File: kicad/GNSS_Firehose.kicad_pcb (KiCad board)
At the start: 4 copper layers, 117.9 x 99.1 mm, 474 parts, among them J1 SMA, J10 HEADER_16, J2 SMA, J3 SMA, J4 SMA, J5 SMA, J6 HEADER_14, J7 L829-1J1T-43, J8 PJ-063BH, Q1 Si2369DS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

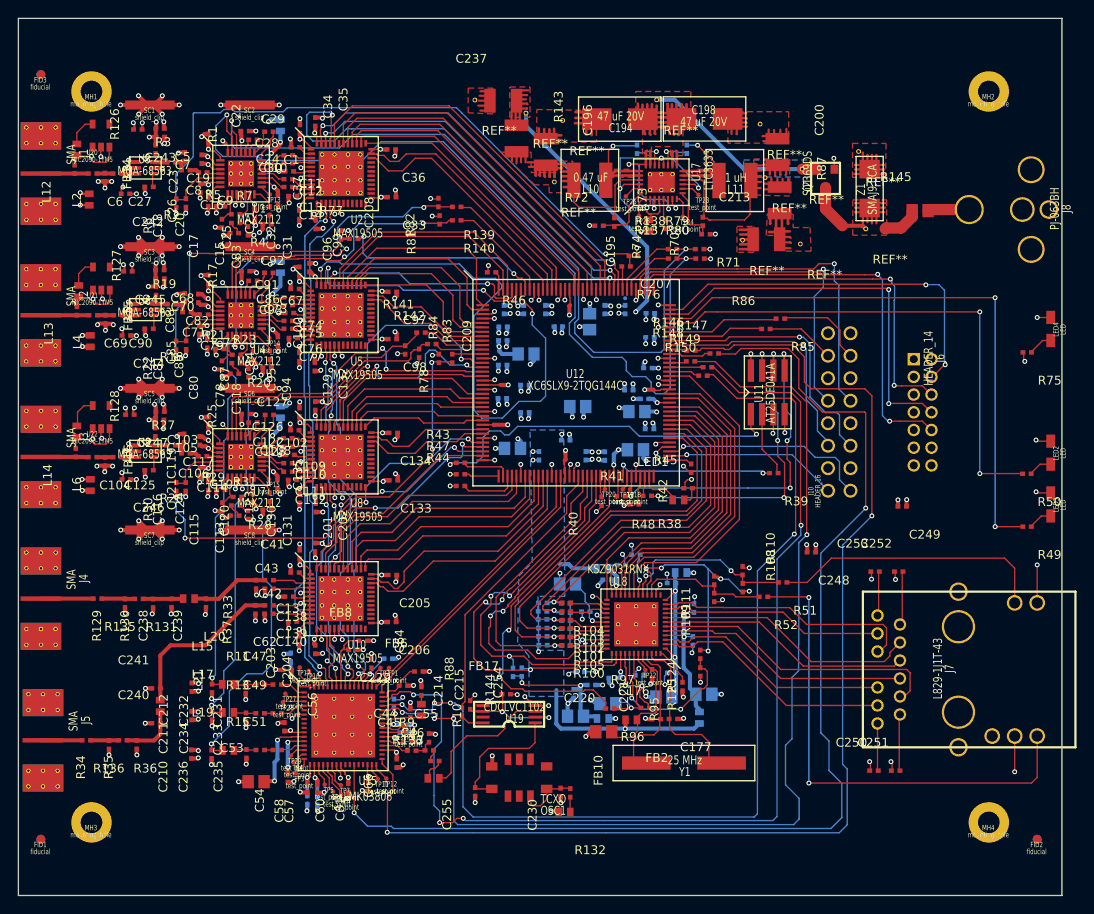
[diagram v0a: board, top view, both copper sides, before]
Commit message: adjust polygons to be close to former gEDA layout
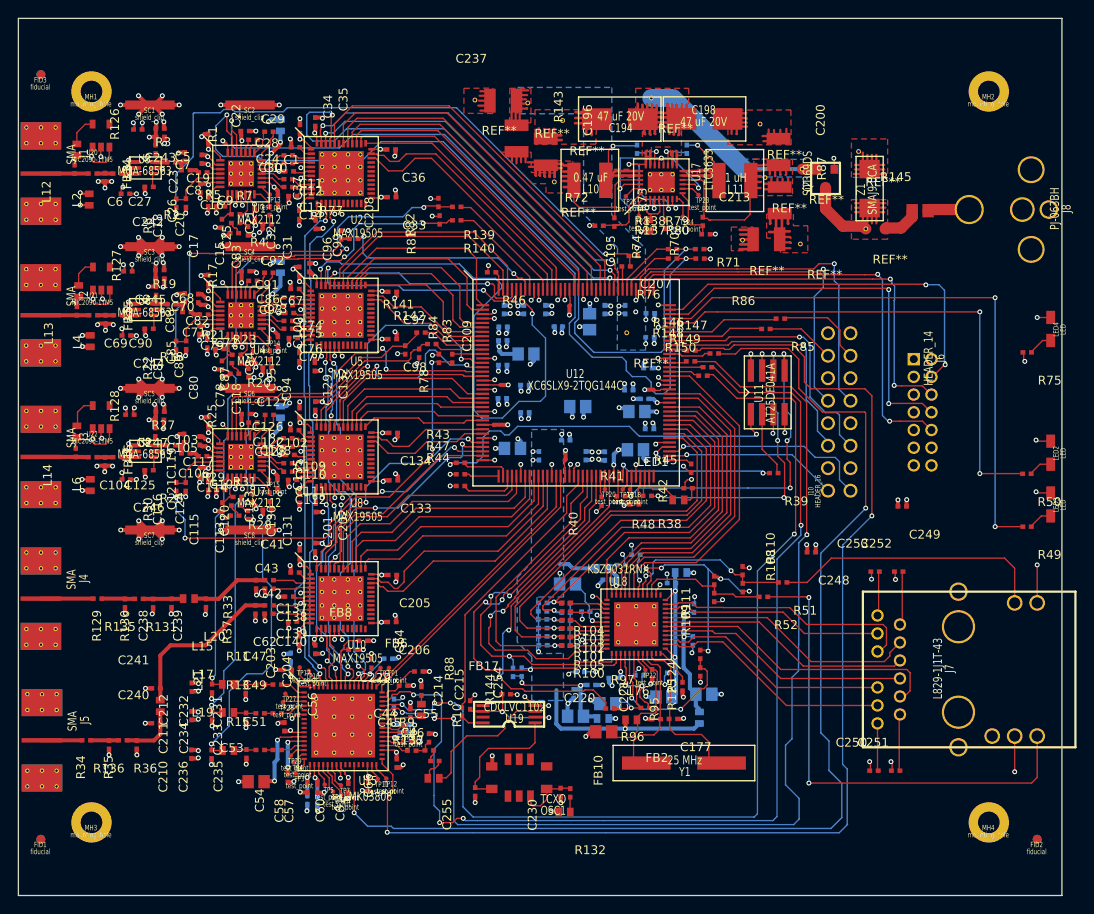
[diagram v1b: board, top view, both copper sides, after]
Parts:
- added REF**: via_12mil, footprints:via_12mil, F.Cu at (142.4, 78.7)
- moved REF** 1.16 mm to (131.2, 52.7)
- moved REF** 0.64 mm to (145.1, 52.2)
- moved C200 0.13 mm to (159.5, 58.3)
- moved J5 0.11 mm to (73.3, 124.7)
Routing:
- net VCC_1.2V: track 88.1 -> 59.4 mm, vias 13 -> 12
- net Net-(C194-Pad1): track 60.5 -> 61.1 mm
- net Net-(Q1-Pad3): track 21.9 -> 22.4 mm
- net (no net): track 0.39 -> 0.00 mm, vias 0 -> 1
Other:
- net class Default: clearance 0.00508 -> 0.14986
- net class wide: clearance 0.00508 -> 0.14986
- rule trace_clearance: 0.00508 -> 0.14986

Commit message: more adjustments on copper layers
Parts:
- removed the REF** at (168.6, 58.2)
- added REF**: via_12mil, footprints:via_12mil, F.Cu at (159.9, 54.2)
- added REF**: via_12mil, footprints:via_12mil, F.Cu at (161.1, 67.2)
- added REF**: via_12mil, footprints:via_12mil, F.Cu at (161.6, 68.2)
- added REF**: via_12mil, footprints:via_12mil, F.Cu at (161.0, 69.1)
- added REF**: via_12mil, footprints:via_12mil, F.Cu at (169.8, 67.5)
- added REF**: via_12mil, footprints:via_12mil, F.Cu at (170.6, 66.6)
- added REF**: via_12mil, footprints:via_12mil, F.Cu at (170.7, 58.4)
- added REF**: via_12mil, footprints:via_12mil, F.Cu at (169.8, 57.6)
- added REF**: via_12mil, footprints:via_12mil, F.Cu at (136.9, 56.7)
- added REF**: via_12mil, footprints:via_12mil, F.Cu at (168.9, 58.4)
- added REF**: via_12mil, footprints:via_12mil, F.Cu at (135.6, 56.7)
- added REF**: via_12mil, footprints:via_12mil, F.Cu at (158.9, 55.2)
- added REF**: via_12mil, footprints:via_12mil, F.Cu at (132.8, 54.2)
- added REF**: via_12mil, footprints:via_12mil, F.Cu at (133.7, 55.1)
- added REF**: via_12mil, footprints:via_12mil, F.Cu at (134.6, 54.2)
- added REF**: via_12mil, footprints:via_12mil, F.Cu at (135.1, 55.3)
- added REF**: via_12mil, footprints:via_12mil, F.Cu at (125.5, 53.5)
- added REF**: via_12mil, footprints:via_12mil, F.Cu at (124.5, 53.5)
- added REF**: via_12mil, footprints:via_12mil, F.Cu at (125.6, 51.6)
- added REF**: via_12mil, footprints:via_12mil, F.Cu at (124.5, 51.6)
- added REF**: via_12mil, footprints:via_12mil, F.Cu at (158.2, 54.2)
- added REF**: via_12mil, footprints:via_12mil, F.Cu at (156.4, 54.1)
- added REF**: via_12mil, footprints:via_12mil, F.Cu at (132.8, 90.7)
- added REF**: via_12mil, footprints:via_12mil, F.Cu at (156.4, 56.5)
- added REF**: via_12mil, footprints:via_12mil, F.Cu at (154.6, 67.2)
- added REF**: via_12mil, footprints:via_12mil, F.Cu at (154.6, 68.5)
- added REF**: via_12mil, footprints:via_12mil, F.Cu at (155.1, 69.1)
- added REF**: via_12mil, footprints:via_12mil, F.Cu at (162.2, 67.2)
- moved REF** 0.81 mm to (135.9, 54.4)
- moved REF** 0.54 mm to (155.1, 67.8)
- moved REF** 0.47 mm to (162.2, 69.1)
- moved REF** 0.41 mm to (169.0, 66.8)
- moved REF** 0.30 mm to (125.0, 52.6)
- moved FID2 0.25 mm to (189.0, 135.9)
- moved REF** 0.20 mm to (157.2, 55.1)
- moved J5 0.13 mm to (73.2, 124.7)
- turned C141 to 180 degrees
- turned C142 to 180 degrees
- turned C143 to 180 degrees
- turned C144 to 180 degrees
- turned C145 to 180 degrees
- turned C146 to 180 degrees
- turned C154 to 180 degrees
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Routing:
- net GND: track 429.9 -> 428.0 mm
- net VCC_3.3V: track 164.6 -> 163.0 mm
- net /RF channel 1/ch1_vcc_lna: track 11.8 -> 12.5 mm
- net /RF Channel 2/ch2_vcc_lna: track 11.7 -> 12.3 mm
- added copper zone on In2.Cu, net /Ethernet/chassis_gnd
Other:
- rule pad_to_mask_clearance: 0.0635 -> 0.0762
- board text added: "P/N 1002-01 REV 2.2"

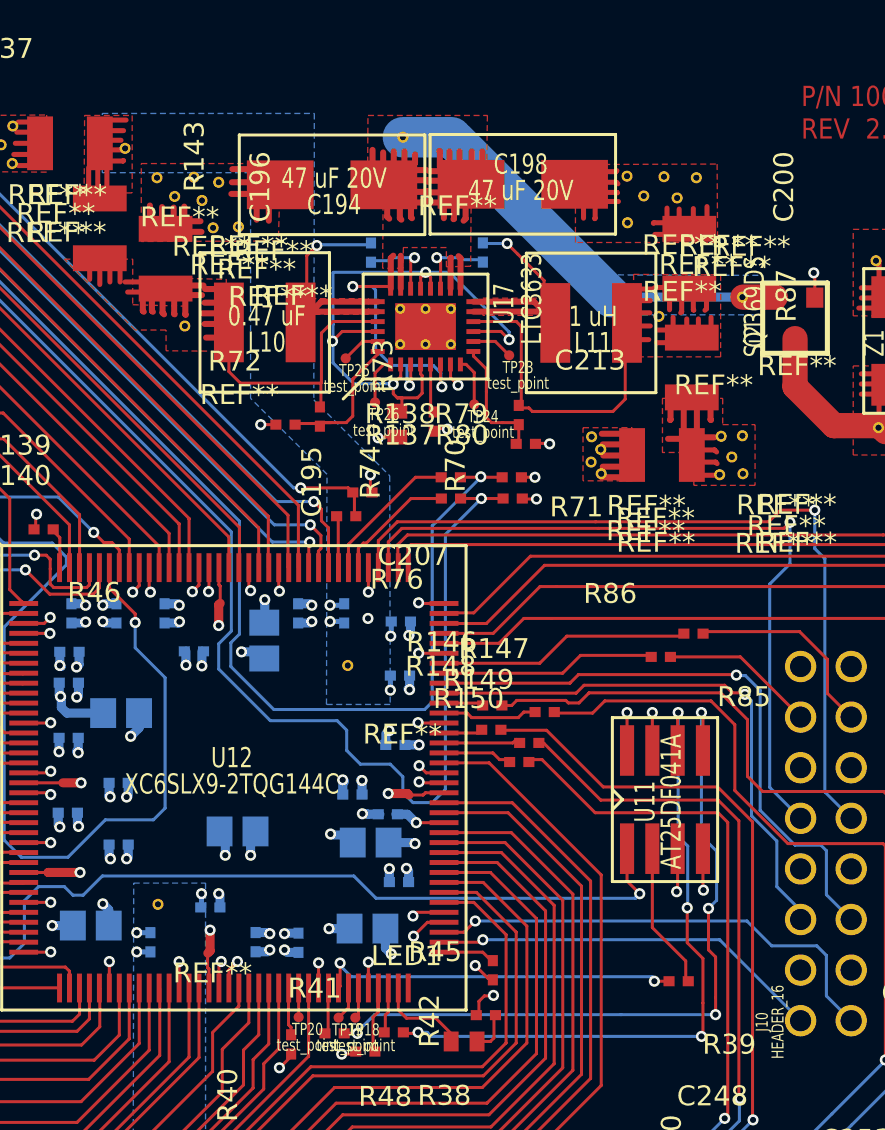
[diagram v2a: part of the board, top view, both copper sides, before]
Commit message: adjust soldermask features
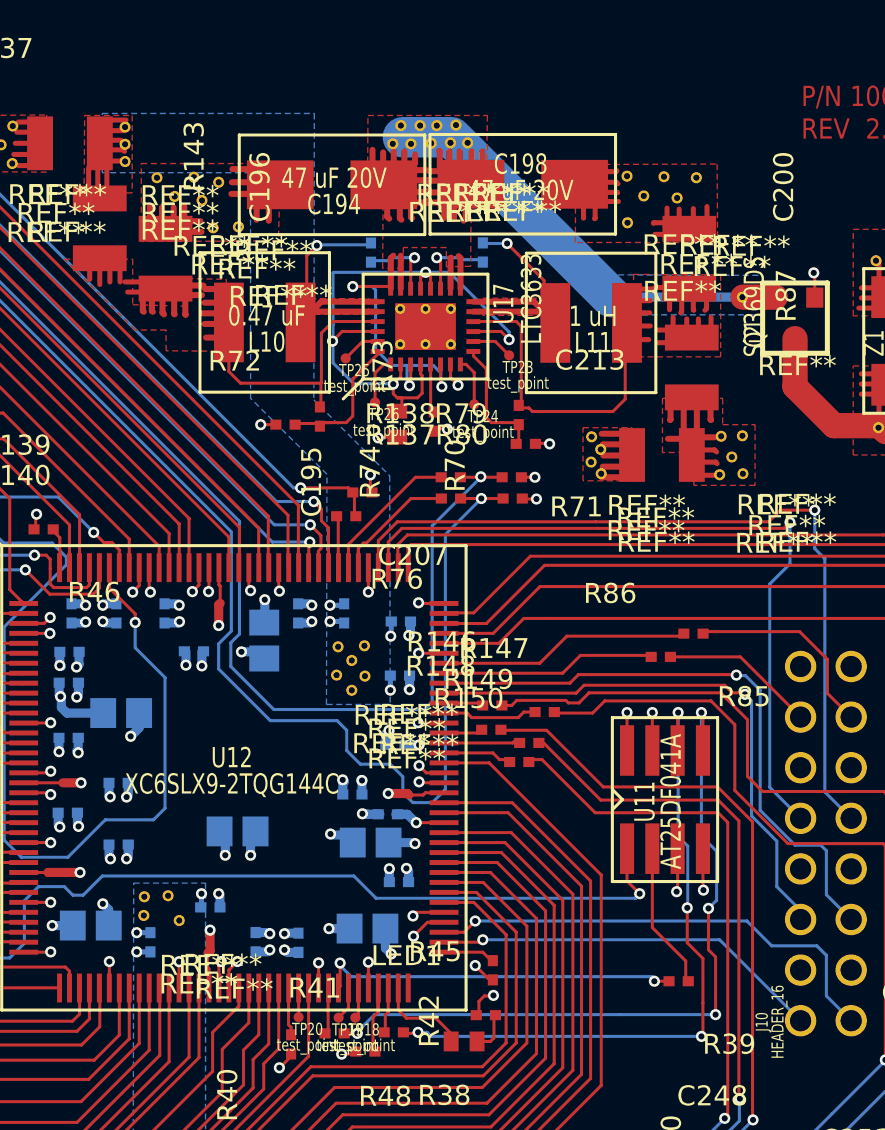
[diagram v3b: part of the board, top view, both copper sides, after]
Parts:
- removed the REF** at (158.0, 61.2)
- removed the REF** at (134.2, 61.6)
- added REF**: via_12mil, footprints:via_12mil, F.Cu at (142.6, 79.9)
- added REF**: via_12mil, footprints:via_12mil, F.Cu at (147.8, 51.6)
- added REF**: via_12mil, footprints:via_12mil, F.Cu at (147.5, 52.5)
- added REF**: via_12mil, footprints:via_12mil, F.Cu at (146.8, 51.6)
- added REF**: via_12mil, footprints:via_12mil, F.Cu at (146.6, 52.5)
- added REF**: via_12mil, footprints:via_12mil, F.Cu at (146.0, 51.6)
- added REF**: via_12mil, footprints:via_12mil, F.Cu at (145.5, 52.5)
- added REF**: via_12mil, footprints:via_12mil, F.Cu at (145.0, 51.6)
- added REF**: via_12mil, footprints:via_12mil, F.Cu at (131.2, 53.4)
- added REF**: via_12mil, footprints:via_12mil, F.Cu at (131.2, 51.7)
- added REF**: via_12mil, footprints:via_12mil, F.Cu at (132.1, 91.2)
- added REF**: via_12mil, footprints:via_12mil, F.Cu at (133.3, 90.2)
- added REF**: via_12mil, footprints:via_12mil, F.Cu at (132.2, 90.3)
- added REF**: via_12mil, footprints:via_12mil, F.Cu at (143.2, 79.2)
- added REF**: via_12mil, footprints:via_12mil, F.Cu at (141.8, 79.2)
- added REF**: via_12mil, footprints:via_12mil, F.Cu at (143.2, 77.7)
- added REF**: via_12mil, footprints:via_12mil, F.Cu at (141.9, 77.7)
- added REF**: via_12mil, footprints:via_12mil, F.Cu at (148.4, 52.5)
- moved REF** 1.34 mm to (133.9, 91.5)
- moved REF** 0.61 mm to (144.6, 52.5)
- moved REF** 0.33 mm to (142.6, 78.4)
- moved REF** 0.20 mm to (131.2, 52.5)
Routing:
- net (no net): vias 1 -> 0
